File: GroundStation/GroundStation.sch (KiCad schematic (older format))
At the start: 8 parts, among them P1 CONN_01X02, U1 ARDUPROMINI, U2 RFM95, U3 LM2596_DC-DC

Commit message: Fix Ground station <3
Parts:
- added P2: CONN_01X02, Pin_Headers:Pin_Header_Straight_1x02, symbol CONN_01X02
- D1: value D -> 1N400x
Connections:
- net at U3.1 (IN+): now also P2.2 (P2); no longer D1.1 (K)
- new net: D1.1 (K), P2.1 (P1)
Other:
- moved on the sheet: D1, P1
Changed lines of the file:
@@
 LIBS:contrib
 LIBS:valves
-LIBS:earth station-cache
+LIBS:GroundStation-cache
 EELAYER 25 0
 EELAYER END
@@
 $EndComp
 $Comp
-L CONN_01X02 P1
-U 1 1 57A635FB
-P 1980 2780
-F 0 "P1" H 1980 2930 50  0000 C CNN
-F 1 "CONN_01X02" V 2080 2780 50  0000 C CNN
-F 2 "Connect:bornier2" H 1980 2780 60  0001 C CNN
-F 3 "" H 1980 2780 60  0000 C CNN
-	1    1980 2780
-	-1   0    0    1
-$EndComp
-$Comp
 L D D2
 U 1 1 57A65CF7
@@
 $EndComp
 $Comp
-L (+3.3) #PWR010
+L (+3.3) #PWR01
 U 1 1 57A66070
 P 4420 4945
-F 0 "#PWR010" H 4420 4995 30  0001 C CNN
+F 0 "#PWR01" H 4420 4995 30  0001 C CNN
 F 1 "(+3.3)" H 4420 5045 50  0000 C CNN
 F 2 "" H 4420 4945 60  0000 C CNN
@@
 	4420 5065 4420 4945
 $Comp
-L (+3.3) #PWR011
+L (+3.3) #PWR02
 U 1 1 57A6619D
 P 4155 2615
-F 0 "#PWR011" H 4155 2665 30  0001 C CNN
+F 0 "#PWR02" H 4155 2665 30  0001 C CNN
 F 1 "(+3.3)" H 4155 2715 50  0000 C CNN
 F 2 "" H 4155 2615 60  0000 C CNN
@@
 $EndComp
 $Comp
-L (+3.3) #PWR012
+L (+3.3) #PWR03
 U 1 1 57A66397
 P 5005 2400
-F 0 "#PWR012" H 5005 2450 30  0001 C CNN
+F 0 "#PWR03" H 5005 2450 30  0001 C CNN
 F 1 "(+3.3)" H 5005 2500 50  0000 C CNN
 F 2 "" H 5005 2400 60  0000 C CNN
@@
 Wire Wire Line
 	4170 2890 4170 2955
-$Comp
-L D D1
-U 1 1 57A68239
-P 2360 2730
-F 0 "D1" H 2360 2830 50  0000 C CNN
-F 1 "D" H 2360 2630 50  0000 C CNN
-F 2 "Diodes_ThroughHole:Diode_DO-41_SOD81_Horizontal_RM10" H 2360 2730 60  0001 C CNN
-F 3 "" H 2360 2730 60  0000 C CNN
-	1    2360 2730
-	-1   0    0    1
-$EndComp
-Wire Wire Line
-	2510 2730 2580 2730
-Wire Wire Line
-	2580 2730 2580 2690
-Wire Wire Line
-	2580 2690 2600 2690
-Wire Wire Line
-	2180 2730 2210 2730
+Wire Wire Line
+	2430 2690 2600 2690
+Wire Wire Line
+	1860 2690 1890 2690
 Wire Wire Line
 	2505 2945 2505 2840
@@
 	2505 2840 2600 2840
 Wire Wire Line
-	2255 2940 2255 2830
-Wire Wire Line
-	2255 2830 2180 2830
+	1935 2900 1935 2790
+Wire Wire Line
+	1935 2790 1860 2790
 Wire Wire Line
 	4155 2690 4100 2690
 $Comp
-L VCC #PWR016
+L VCC #PWR04
 U 1 1 57A6A0CA
 P 3870 4990
-F 0 "#PWR016" H 3870 5040 30  0001 C CNN
+F 0 "#PWR04" H 3870 5040 30  0001 C CNN
 F 1 "VCC" H 3870 5090 50  0000 C CNN
 F 2 "" H 3870 4990 60  0000 C CNN
@@
 Connection ~ 3870 5065
 $Comp
-L VCC #PWR017
+L VCC #PWR05
 U 1 1 57A6A201
 P 7255 2445
-F 0 "#PWR017" H 7255 2495 30  0001 C CNN
+F 0 "#PWR05" H 7255 2495 30  0001 C CNN
 F 1 "VCC" H 7255 2545 50  0000 C CNN
 F 2 "" H 7255 2445 60  0000 C CNN
@@
 $EndComp
 $Comp
-L GND #PWR?
+L GND #PWR06
 U 1 1 57C8B7E1
 P 5005 2860
-F 0 "#PWR?" H 5005 2610 50  0001 C CNN
+F 0 "#PWR06" H 5005 2610 50  0001 C CNN
 F 1 "GND" H 5005 2710 50  0000 C CNN
 F 2 "" H 5005 2860 50  0000 C CNN
@@
 $EndComp
 $Comp
-L GND #PWR?
+L GND #PWR07
 U 1 1 57C8B979
 P 5620 3010
-F 0 "#PWR?" H 5620 2760 50  0001 C CNN
+F 0 "#PWR07" H 5620 2760 50  0001 C CNN
 F 1 "GND" H 5620 2860 50  0000 C CNN
 F 2 "" H 5620 3010 50  0000 C CNN
@@
 $EndComp
 $Comp
-L GND #PWR?
+L GND #PWR08
 U 1 1 57C8B99C
 P 4170 2955
-F 0 "#PWR?" H 4170 2705 50  0001 C CNN
+F 0 "#PWR08" H 4170 2705 50  0001 C CNN
 F 1 "GND" H 4170 2805 50  0000 C CNN
 F 2 "" H 4170 2955 50  0000 C CNN
@@
 $EndComp
 $Comp
-L GND #PWR?
+L GND #PWR09
 U 1 1 57C8BB2F
 P 2505 2945
-F 0 "#PWR?" H 2505 2695 50  0001 C CNN
+F 0 "#PWR09" H 2505 2695 50  0001 C CNN
 F 1 "GND" H 2505 2795 50  0000 C CNN
 F 2 "" H 2505 2945 50  0000 C CNN
@@
 $EndComp
 $Comp
-L GND #PWR?
+L GND #PWR010
 U 1 1 57C8BC8A
-P 2255 2940
-F 0 "#PWR?" H 2255 2690 50  0001 C CNN
-F 1 "GND" H 2255 2790 50  0000 C CNN
-F 2 "" H 2255 2940 50  0000 C CNN
-F 3 "" H 2255 2940 50  0000 C CNN
-	1    2255 2940
-	1    0    0    -1
-$EndComp
-$Comp
-L GND #PWR?
+P 1935 2900
+F 0 "#PWR010" H 1935 2650 50  0001 C CNN
+F 1 "GND" H 1935 2750 50  0000 C CNN
+F 2 "" H 1935 2900 50  0000 C CNN
+F 3 "" H 1935 2900 50  0000 C CNN
+	1    1935 2900
+	1    0    0    -1
+$EndComp
+$Comp
+L GND #PWR011
 U 1 1 57C8BCAD
 P 2280 5150
-F 0 "#PWR?" H 2280 4900 50  0001 C CNN
+F 0 "#PWR011" H 2280 4900 50  0001 C CNN
 F 1 "GND" H 2280 5000 50  0000 C CNN
 F 2 "" H 2280 5150 50  0000 C CNN
@@
 $EndComp
 $Comp
-L GND #PWR?
+L GND #PWR012
 U 1 1 57C8BEA0
 P 7130 2800
-F 0 "#PWR?" H 7130 2550 50  0001 C CNN
+F 0 "#PWR012" H 7130 2550 50  0001 C CNN
 F 1 "GND" H 7130 2650 50  0000 C CNN
 F 2 "" H 7130 2800 50  0000 C CNN
@@
 	6985 2850 6830 2850
 $Comp
-L GND #PWR?
+L GND #PWR013
 U 1 1 57C8C5CE
 P 5570 2175
-F 0 "#PWR?" H 5570 1925 50  0001 C CNN
+F 0 "#PWR013" H 5570 1925 50  0001 C CNN
 F 1 "GND" H 5570 2025 50  0000 C CNN
 F 2 "" H 5570 2175 50  0000 C CNN
@@
 	5630 2175 5570 2175
 $Comp
-L GND #PWR?
+L GND #PWR014
 U 1 1 57C8C6EF
 P 7395 3350
-F 0 "#PWR?" H 7395 3100 50  0001 C CNN
+F 0 "#PWR014" H 7395 3100 50  0001 C CNN
 F 1 "GND" H 7395 3200 50  0000 C CNN
 F 2 "" H 7395 3350 50  0000 C CNN
@@
 $EndComp
 $Comp
-L GND #PWR?
+L GND #PWR015
 U 1 1 57C8C7C2
 P 7545 3350
-F 0 "#PWR?" H 7545 3100 50  0001 C CNN
+F 0 "#PWR015" H 7545 3100 50  0001 C CNN
 F 1 "GND" H 7545 3200 50  0000 C CNN
 F 2 "" H 7545 3350 50  0000 C CNN
@@
 $EndComp
 $Comp
-L GND #PWR?
+L GND #PWR016
 U 1 1 57C8C7E5
 P 7395 2650
-F 0 "#PWR?" H 7395 2400 50  0001 C CNN
+F 0 "#PWR016" H 7395 2400 50  0001 C CNN
 F 1 "GND" H 7395 2500 50  0000 C CNN
 F 2 "" H 7395 2650 50  0000 C CNN
@@
 $EndComp
 $Comp
-L GND #PWR?
+L GND #PWR017
 U 1 1 57C8C8F8
 P 7545 2650
-F 0 "#PWR?" H 7545 2400 50  0001 C CNN
+F 0 "#PWR017" H 7545 2400 50  0001 C CNN
 F 1 "GND" H 7545 2500 50  0000 C CNN
 F 2 "" H 7545 2650 50  0000 C CNN
@@
 	-1   0    0    1
 $EndComp
+$Comp
+L CONN_01X02 P1
+U 1 1 57A635FB
+P 1660 2740
+F 0 "P1" H 1660 2890 50  0000 C CNN
+F 1 "CONN_01X02" V 1760 2740 50  0000 C CNN
+F 2 "Connect:bornier2" H 1660 2740 60  0001 C CNN
+F 3 "" H 1660 2740 60  0000 C CNN
+	1    1660 2740
+	-1   0    0    1
+$EndComp
+$Comp
+L D D1
+U 1 1 57A68239
+P 2040 2690
+F 0 "D1" H 2040 2790 50  0000 C CNN
+F 1 "1N400x" H 2040 2590 50  0000 C CNN
+F 2 "Diodes_ThroughHole:Diode_DO-41_SOD81_Horizontal_RM10" H 2040 2690 60  0001 C CNN
+F 3 "" H 2040 2690 60  0000 C CNN
+	1    2040 2690
+	-1   0    0    1
+$EndComp
+$Comp
+L CONN_01X02 P2
+U 1 1 580582E7
+P 2380 2340
+F 0 "P2" H 2380 2490 50  0000 C CNN
+F 1 "CONN_01X02" V 2480 2340 50  0000 C CNN
+F 2 "Pin_Headers:Pin_Header_Straight_1x02" H 2380 2340 50  0001 C CNN
+F 3 "" H 2380 2340 50  0000 C CNN
+	1    2380 2340
+	0    -1   -1   0
+$EndComp
+Wire Wire Line
+	2430 2540 2430 2690
+Wire Wire Line
+	2330 2540 2330 2690
+Wire Wire Line
+	2330 2690 2190 2690
 $EndSCHEMATC

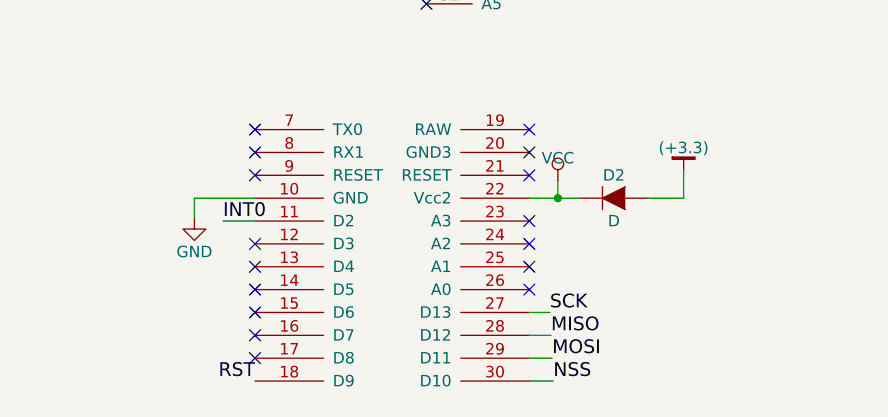
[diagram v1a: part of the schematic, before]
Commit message: Add extra I/O pins Ground station
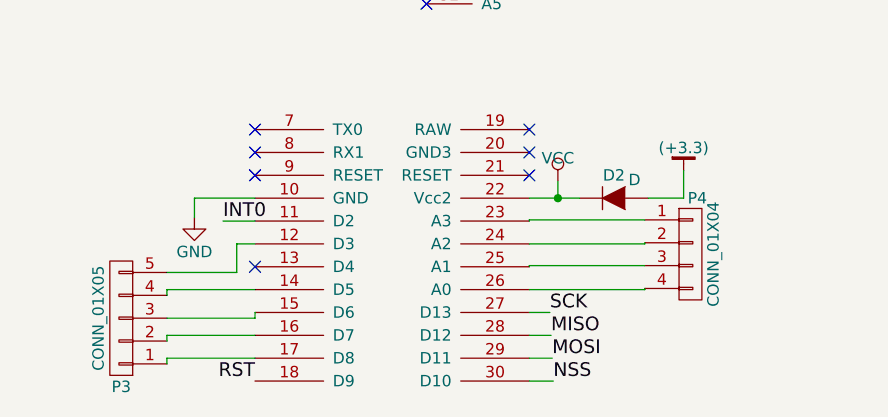
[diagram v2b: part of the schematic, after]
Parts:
- added P3: CONN_01X05, symbol CONN_01X05
- added P4: CONN_01X04, symbol CONN_01X04
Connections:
- net at U1.12 (D3): now also P3.5 (P5)
- net at U1.14 (D5): now also P3.4 (P4)
- net at U1.15 (D6): now also P3.3 (P3)
- net at U1.16 (D7): now also P3.2 (P2)
- net at U1.17 (D8): now also P3.1 (P1)
- net at U1.23 (A3): now also P4.1 (P1)
- net at U1.24 (A2): now also P4.2 (P2)
- net at U1.25 (A1): now also P4.3 (P3)
- net at U1.26 (A0): now also P4.4 (P4)
- no-connect marks 23 -> 14
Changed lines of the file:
@@
 NoConn ~ 2545 4765
 NoConn ~ 2545 4865
-NoConn ~ 3745 5165
-NoConn ~ 3745 5265
-NoConn ~ 3745 5365
-NoConn ~ 3745 5465
 Text Label 6925 2450 0    60   ~ 0
 INT0
@@
 NoConn ~ 3295 4115
 NoConn ~ 3295 4215
-NoConn ~ 2545 5265
 NoConn ~ 2545 5365
-NoConn ~ 2545 5465
-NoConn ~ 2545 5565
-NoConn ~ 2545 5665
-NoConn ~ 2545 5765
 NoConn ~ 3745 4765
 NoConn ~ 3745 4865
@@
 NoConn ~ 2545 4965
 $Comp
-L ARDUPROMINI U1
-U 1 1 57A10FE7
-P 3745 3665
-F 0 "U1" H 3545 3565 60  0000 C CNN
-F 1 "ARDUPROMINI" H 3745 3665 60  0000 C CNN
-F 2 "CatSat:arduinoMiniPro2" H 3745 3665 60  0001 C CNN
-F 3 "" H 3745 3665 60  0000 C CNN
-	1    3745 3665
-	1    0    0    -1
-$EndComp
-$Comp
 L D D2
 U 1 1 57A65CF7
 P 4115 5065
 F 0 "D2" H 4115 5165 50  0000 C CNN
-F 1 "D" H 4115 4965 50  0000 C CNN
+F 1 "D" H 4205 5145 50  0000 C CNN
 F 2 "Diodes_ThroughHole:Diode_DO-41_SOD81_Horizontal_RM10" H 4115 5065 60  0001 C CNN
 F 3 "" H 4115 5065 60  0000 C CNN
@@
 $EndComp
 $Comp
-L (+3.3) #PWR01
+L (+3.3) #PWR7
 U 1 1 57A66070
 P 4420 4945
-F 0 "#PWR01" H 4420 4995 30  0001 C CNN
+F 0 "#PWR7" H 4420 4995 30  0001 C CNN
 F 1 "(+3.3)" H 4420 5045 50  0000 C CNN
 F 2 "" H 4420 4945 60  0000 C CNN
@@
 	4420 5065 4420 4945
 $Comp
-L (+3.3) #PWR02
+L (+3.3) #PWR5
 U 1 1 57A6619D
 P 4155 2615
-F 0 "#PWR02" H 4155 2665 30  0001 C CNN
+F 0 "#PWR5" H 4155 2665 30  0001 C CNN
 F 1 "(+3.3)" H 4155 2715 50  0000 C CNN
 F 2 "" H 4155 2615 60  0000 C CNN
@@
 $EndComp
 $Comp
-L (+3.3) #PWR03
+L (+3.3) #PWR8
 U 1 1 57A66397
 P 5005 2400
-F 0 "#PWR03" H 5005 2450 30  0001 C CNN
+F 0 "#PWR8" H 5005 2450 30  0001 C CNN
 F 1 "(+3.3)" H 5005 2500 50  0000 C CNN
 F 2 "" H 5005 2400 60  0000 C CNN
@@
 	4155 2690 4100 2690
 $Comp
-L VCC #PWR04
+L VCC #PWR4
 U 1 1 57A6A0CA
 P 3870 4990
-F 0 "#PWR04" H 3870 5040 30  0001 C CNN
+F 0 "#PWR4" H 3870 5040 30  0001 C CNN
 F 1 "VCC" H 3870 5090 50  0000 C CNN
 F 2 "" H 3870 4990 60  0000 C CNN
@@
 Connection ~ 3870 5065
 $Comp
-L VCC #PWR05
+L VCC #PWR13
 U 1 1 57A6A201
 P 7255 2445
-F 0 "#PWR05" H 7255 2495 30  0001 C CNN
+F 0 "#PWR13" H 7255 2495 30  0001 C CNN
 F 1 "VCC" H 7255 2545 50  0000 C CNN
 F 2 "" H 7255 2445 60  0000 C CNN
@@
 $EndComp
 $Comp
-L GND #PWR06
+L GND #PWR9
 U 1 1 57C8B7E1
 P 5005 2860
-F 0 "#PWR06" H 5005 2610 50  0001 C CNN
+F 0 "#PWR9" H 5005 2610 50  0001 C CNN
 F 1 "GND" H 5005 2710 50  0000 C CNN
 F 2 "" H 5005 2860 50  0000 C CNN
@@
 $EndComp
 $Comp
-L GND #PWR07
+L GND #PWR11
 U 1 1 57C8B979
 P 5620 3010
-F 0 "#PWR07" H 5620 2760 50  0001 C CNN
+F 0 "#PWR11" H 5620 2760 50  0001 C CNN
 F 1 "GND" H 5620 2860 50  0000 C CNN
 F 2 "" H 5620 3010 50  0000 C CNN
@@
 $EndComp
 $Comp
-L GND #PWR08
+L GND #PWR6
 U 1 1 57C8B99C
 P 4170 2955
-F 0 "#PWR08" H 4170 2705 50  0001 C CNN
+F 0 "#PWR6" H 4170 2705 50  0001 C CNN
 F 1 "GND" H 4170 2805 50  0000 C CNN
 F 2 "" H 4170 2955 50  0000 C CNN
@@
 $EndComp
 $Comp
-L GND #PWR09
+L GND #PWR3
 U 1 1 57C8BB2F
 P 2505 2945
-F 0 "#PWR09" H 2505 2695 50  0001 C CNN
+F 0 "#PWR3" H 2505 2695 50  0001 C CNN
 F 1 "GND" H 2505 2795 50  0000 C CNN
 F 2 "" H 2505 2945 50  0000 C CNN
@@
 $EndComp
 $Comp
-L GND #PWR010
+L GND #PWR1
 U 1 1 57C8BC8A
 P 1935 2900
-F 0 "#PWR010" H 1935 2650 50  0001 C CNN
+F 0 "#PWR1" H 1935 2650 50  0001 C CNN
 F 1 "GND" H 1935 2750 50  0000 C CNN
 F 2 "" H 1935 2900 50  0000 C CNN
@@
 $EndComp
 $Comp
-L GND #PWR011
+L GND #PWR2
 U 1 1 57C8BCAD
 P 2280 5150
-F 0 "#PWR011" H 2280 4900 50  0001 C CNN
+F 0 "#PWR2" H 2280 4900 50  0001 C CNN
 F 1 "GND" H 2280 5000 50  0000 C CNN
 F 2 "" H 2280 5150 50  0000 C CNN
@@
 $EndComp
 $Comp
-L GND #PWR012
+L GND #PWR12
 U 1 1 57C8BEA0
 P 7130 2800
-F 0 "#PWR012" H 7130 2550 50  0001 C CNN
+F 0 "#PWR12" H 7130 2550 50  0001 C CNN
 F 1 "GND" H 7130 2650 50  0000 C CNN
 F 2 "" H 7130 2800 50  0000 C CNN
@@
 	6985 2850 6830 2850
 $Comp
-L GND #PWR013
+L GND #PWR10
 U 1 1 57C8C5CE
 P 5570 2175
-F 0 "#PWR013" H 5570 1925 50  0001 C CNN
+F 0 "#PWR10" H 5570 1925 50  0001 C CNN
 F 1 "GND" H 5570 2025 50  0000 C CNN
 F 2 "" H 5570 2175 50  0000 C CNN
@@
 	5630 2175 5570 2175
 $Comp
-L GND #PWR014
+L GND #PWR15
 U 1 1 57C8C6EF
 P 7395 3350
-F 0 "#PWR014" H 7395 3100 50  0001 C CNN
+F 0 "#PWR15" H 7395 3100 50  0001 C CNN
 F 1 "GND" H 7395 3200 50  0000 C CNN
 F 2 "" H 7395 3350 50  0000 C CNN
@@
 $EndComp
 $Comp
-L GND #PWR015
+L GND #PWR17
 U 1 1 57C8C7C2
 P 7545 3350
-F 0 "#PWR015" H 7545 3100 50  0001 C CNN
+F 0 "#PWR17" H 7545 3100 50  0001 C CNN
 F 1 "GND" H 7545 3200 50  0000 C CNN
 F 2 "" H 7545 3350 50  0000 C CNN
@@
 $EndComp
 $Comp
-L GND #PWR016
+L GND #PWR14
 U 1 1 57C8C7E5
 P 7395 2650
-F 0 "#PWR016" H 7395 2400 50  0001 C CNN
+F 0 "#PWR14" H 7395 2400 50  0001 C CNN
 F 1 "GND" H 7395 2500 50  0000 C CNN
 F 2 "" H 7395 2650 50  0000 C CNN
@@
 $EndComp
 $Comp
-L GND #PWR017
+L GND #PWR16
 U 1 1 57C8C8F8
 P 7545 2650
-F 0 "#PWR017" H 7545 2400 50  0001 C CNN
+F 0 "#PWR16" H 7545 2400 50  0001 C CNN
 F 1 "GND" H 7545 2500 50  0000 C CNN
 F 2 "" H 7545 2650 50  0000 C CNN
@@
 Wire Wire Line
 	2330 2690 2190 2690
+$Comp
+L ARDUPROMINI U1
+U 1 1 57A10FE7
+P 3745 3665
+F 0 "U1" H 3545 3565 60  0000 C CNN
+F 1 "ARDUPROMINI" H 3745 3665 60  0000 C CNN
+F 2 "CatSat:arduinoMiniPro2" H 3745 3665 60  0001 C CNN
+F 3 "" H 3745 3665 60  0000 C CNN
+	1    3745 3665
+	1    0    0    -1
+$EndComp
+$Comp
+L CONN_01X05 P3
+U 1 1 5805A2F2
+P 1960 5590
+F 0 "P3" H 1960 5890 50  0000 C CNN
+F 1 "CONN_01X05" V 2060 5590 50  0000 C CNN
+F 2 "" H 1960 5590 50  0000 C CNN
+F 3 "" H 1960 5590 50  0000 C CNN
+	1    1960 5590
+	-1   0    0    1
+$EndComp
+$Comp
+L CONN_01X04 P4
+U 1 1 5805A3F8
+P 4450 5310
+F 0 "P4" H 4480 5555 50  0000 C CNN
+F 1 "CONN_01X04" V 4550 5310 50  0000 C CNN
+F 2 "" H 4450 5310 50  0000 C CNN
+F 3 "" H 4450 5310 50  0000 C CNN
+	1    4450 5310
+	1    0    0    -1
+$EndComp
+Wire Wire Line
+	4250 5160 3745 5160
+Wire Wire Line
+	3745 5160 3745 5165
+Wire Wire Line
+	3745 5265 4250 5265
+Wire Wire Line
+	4250 5265 4250 5260
+Wire Wire Line
+	4250 5360 3745 5360
+Wire Wire Line
+	3745 5360 3745 5365
+Wire Wire Line
+	3745 5465 4250 5465
+Wire Wire Line
+	4250 5465 4250 5460
+Wire Wire Line
+	2160 5390 2465 5390
+Wire Wire Line
+	2465 5390 2465 5265
+Wire Wire Line
+	2465 5265 2545 5265
+Wire Wire Line
+	2545 5465 2160 5465
+Wire Wire Line
+	2160 5465 2160 5490
+Wire Wire Line
+	2545 5590 2545 5565
+Wire Wire Line
+	2160 5590 2545 5590
+Wire Wire Line
+	2545 5665 2160 5665
+Wire Wire Line
+	2160 5665 2160 5690
+Wire Wire Line
+	2545 5765 2160 5765
+Wire Wire Line
+	2160 5765 2160 5790
 $EndSCHEMATC
